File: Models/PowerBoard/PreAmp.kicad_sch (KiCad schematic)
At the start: 14 parts, among them U5 LM7805, 5V, 5%, U6 LM7905, -5V, 5%

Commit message: Should be finished with components BOM
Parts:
- C10, C11: Cost (none) -> $0.078; Purchase Link (none) -> https://www.digikey.com/en/products/detail/murata-electroni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
- C12: Cost (none) -> $0.079; Purchase Link (none) -> https://www.digikey.com/en/products/detail/murata-electroni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
- C13, C14: Cost (none) -> $0.087; Purchase Link (none) -> https://www.digikey.com/en/products/detail/murata-electroni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
- C9: Cost (none) -> $0.074; Purchase Link (none) -> https://www.digikey.com/en/products/detail/murata-electroni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
- D11, D12: Cost (none) -> $0.166; Purchase Link (none) -> https://www.digikey.com/en/products/detail/diodes-incorpora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
- RV1, RV2: Cost (none) -> $2.050; Purchase Link (none) -> https://www.digikey.com/en/products/detail/bourns-inc/3296Y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
- U5: Cost (none) -> $1.800; Purchase Link (none) -> https://www.digikey.com/en/products/detail/texas-instrument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
- U6: Cost (none) -> $1.530; Purchase Link (none) -> https://www.digikey.com/en/products/detail/texas-instrument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
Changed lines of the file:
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@@
+			)
+		)
+		(property "Cost" "$0.078"
+			(at 106.68 118.11 0)
+			(effects
+				(font
+					(size 1.27 1.27)
+				)
+				(hide yes)
+			)
+		)
+		(property "Purchase Link" "https://www.digikey.com/en/products/detail/murata-electronics/GRT188R61H105KE13D/5416752"
+			(at 106.68 118.11 0)
+			(effects
+				(font
+					(size 1.27 1.27)
+				)
+				(hide yes)
 			)
 		)
@@
 			)
 		)
-		(property "Purchase Link" ""
+		(property "Purchase Link" "https://www.digikey.com/en/products/detail/texas-instruments/LM7805CT-NOPB/3901929"
+			(at 68.58 55.88 0)
+			(effects
+				(font
+					(size 1.27 1.27)
+				)
+				(hide yes)
+			)
+		)
+		(property "Cost" "$1.800"
 			(at 68.58 55.88 0)
 			(effects
@@
 			)
 		)
-		(property "Purchase Link" ""
+		(property "Purchase Link" "https://www.digikey.com/en/products/detail/diodes-incorporated/1N5819HW-7-F/814970"
 			(at 129.54 118.11 0)
+			(effects
+				(font
+					(size 1.27 1.27)
+				)
+				(hide yes)
+			)
+		)
+		(property "Cost" "$0.166"
+			(at 129.54 118.11 90)
 			(effects
 				(font
@@
 			)
 		)
-		(property "Purchase Link" ""
+		(property "Purchase Link" "https://www.digikey.com/en/products/detail/murata-electronics/GRT188R61H105KE13D/5416752"
+			(at 106.68 148.59 0)
+			(effects
+				(font
+					(size 1.27 1.27)
+				)
+				(hide yes)
+			)
+		)
+		(property "Cost" "$0.078"
 			(at 106.68 148.59 0)
 			(effects
@@
 			)
 		)
+		(property "Cost" "$0.087"
+			(at 210.82 57.15 0)
+			(effects
+				(font
+					(size 1.27 1.27)
+				)
+				(hide yes)
+			)
+		)
+		(property "Purchase Link" "https://www.digikey.com/en/products/detail/murata-electronics/GRM21BR61E106KA73K/4905532"
+			(at 210.82 57.15 0)
+			(effects
+				(font
+					(size 1.27 1.27)
+				)
+				(hide yes)
+			)
+		)
 		(pin "1"
 		)
@@
 			)
 		)
+		(property "Cost" "$0.079"
+			(at 114.3 67.31 0)
+			(effects
+				(font
+					(size 1.27 1.27)
+				)
+				(hide yes)
+			)
+		)
+		(property "Purchase Link" "https://www.digikey.com/en/products/detail/murata-electronics/GRM188R72A104KA35D/702549"
+			(at 114.3 67.31 0)
+			(effects
+				(font
+					(size 1.27 1.27)
+				)
+				(hide yes)
+			)
+		)
 		(pin "1"
 		)
@@
 			)
 		)
-		(property "Purchase Link" ""
+		(property "Purchase Link" "https://www.digikey.com/en/products/detail/texas-instruments/LM7905CT-NOPB/6349"
+			(at 68.58 132.08 0)
+			(effects
+				(font
+					(size 1.27 1.27)
+				)
+				(hide yes)
+			)
+		)
+		(property "Cost" "$1.530"
 			(at 68.58 132.08 0)
 			(effects
@@
 			)
 		)
+		(property "Cost" "$0.074"
+			(at 66.04 67.31 0)
+			(effects
+				(font
+					(size 1.27 1.27)
+				)
+				(hide yes)
+			)
+		)
+		(property "Purchase Link" "https://www.digikey.com/en/products/detail/murata-electronics/GRM188R71H224KAC4D/5797498"
+			(at 66.04 67.31 0)
+			(effects
+				(font
+					(size 1.27 1.27)
+				)
+				(hide yes)
+			)
+		)
 		(pin "1"
 		)
@@
 		)
 		(property "Description" "Unpolarized capacitor"
+			(at 210.82 110.49 0)
+			(effects
+				(font
+					(size 1.27 1.27)
+				)
+				(hide yes)
+			)
+		)
+		(property "Cost" "$0.087"
+			(at 210.82 110.49 0)
+			(effects
+				(font
+					(size 1.27 1.27)
+				)
+				(hide yes)
+			)
+		)
+		(property "Purchase Link" "https://www.digikey.com/en/products/detail/murata-electronics/GRM21BR61E106KA73K/4905532"
 			(at 210.82 110.49 0)
 			(effects
@@
 			)
 		)
-		(property "Purchase Link" ""
+		(property "Purchase Link" "https://www.digikey.com/en/products/detail/diodes-incorporated/1N5819HW-7-F/814970"
 			(at 137.16 67.31 0)
+			(effects
+				(font
+					(size 1.27 1.27)
+				)
+				(hide yes)
+			)
+		)
+		(property "Cost" "$0.166"
+			(at 137.16 67.31 90)
 			(effects
 				(font
@@
 			)
 		)
+		(property "Cost" "$2.050"
+			(at 203.2 50.8 0)
+			(effects
+				(font
+					(size 1.27 1.27)
+				)
+				(hide yes)
+			)
+		)
+		(property "Purchase Link" "https://www.digikey.com/en/products/detail/bourns-inc/3296Y-1-102LF/1088084"
+			(at 203.2 50.8 0)
+			(effects
+				(font
+					(size 1.27 1.27)
+				)
+				(hide yes)
+			)
+		)
 		(pin "2"
 		)
@@
 			(at 203.2 116.84 0)
 			(effects
+				(font
+					(size 1.27 1.27)
+				)
+				(hide yes)
+			)
+		)
+		(property "Cost" "$2.050"
+			(at 203.2 116.84 0)
+			(effects
+				(font
+					(size 1.27 1.27)
+				)
+				(hide yes)
+			)
+		)
+		(property "Purchase Link" "https://www.digikey.com/en/products/detail/bourns-inc/3296Y-1-102LF/1088084"
+			(at 203.2 116.84 0)
+			(effects

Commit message: Assigned footprints
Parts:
- C10, C11, C12, C9: footprint (none) -> TwoTerminal:CAPC0603
- C13, C14: footprint (none) -> TwoTerminal:CAPC0805
- D10, D9: footprint (none) -> TwoTerminal:SOD-123FL
- D11, D12: footprint (none) -> TwoTerminal:SOD-123
- RV1, RV2: footprint (none) -> ThreeTerminal:Bourns_3296Y
- U5, U6: footprint (none) -> ThreeTerminal:TO-220
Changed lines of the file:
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@@
 			)
 		)
-		(property "Footprint" ""
+		(property "Footprint" "TwoTerminal:CAPC0603"
 			(at 107.6452 121.92 0)
 			(effects
@@
 			)
 		)
-		(property "Footprint" ""
+		(property "Footprint" "ThreeTerminal:TO-220"
 			(at 68.58 55.88 0)
 			(effects
@@
 			)
 		)
-		(property "Footprint" ""
+		(property "Footprint" "TwoTerminal:SOD-123"
 			(at 129.54 118.11 0)
 			(effects
@@
 			)
 		)
-		(property "Footprint" ""
+		(property "Footprint" "TwoTerminal:CAPC0603"
 			(at 107.6452 152.4 0)
 			(effects
@@
 			)
 		)
-		(property "Footprint" ""
+		(property "Footprint" "TwoTerminal:CAPC0805"
 			(at 211.7852 60.96 0)
 			(effects
@@
 			)
 		)
-		(property "Footprint" ""
+		(property "Footprint" "TwoTerminal:SOD-123FL"
 			(at 86.36 38.1 0)
 			(effects
@@
 			)
 		)
-		(property "Footprint" ""
+		(property "Footprint" "TwoTerminal:SOD-123FL"
 			(at 111.76 135.89 0)
 			(effects
@@
 			)
 		)
-		(property "Footprint" ""
+		(property "Footprint" "TwoTerminal:CAPC0603"
 			(at 115.2652 71.12 0)
 			(effects
@@
 			)
 		)
-		(property "Footprint" ""
+		(property "Footprint" "ThreeTerminal:TO-220"
 			(at 68.58 132.08 0)
 			(effects
@@
 			)
 		)
-		(property "Footprint" ""
+		(property "Footprint" "TwoTerminal:CAPC0603"
 			(at 67.0052 71.12 0)
 			(effects
@@
 			)
 		)
-		(property "Footprint" ""
+		(property "Footprint" "TwoTerminal:CAPC0805"
 			(at 211.7852 114.3 0)
 			(effects
@@
 			)
 		)
-		(property "Footprint" ""
+		(property "Footprint" "TwoTerminal:SOD-123"
 			(at 137.16 67.31 0)
 			(effects
@@
 			)
 		)
-		(property "Footprint" ""
+		(property "Footprint" "ThreeTerminal:Bourns_3296Y"
 			(at 203.2 50.8 0)
 			(effects
@@
 			)
 		)
-		(property "Footprint" ""
+		(property "Footprint" "ThreeTerminal:Bourns_3296Y"
 			(at 203.2 116.84 0)
 			(effects

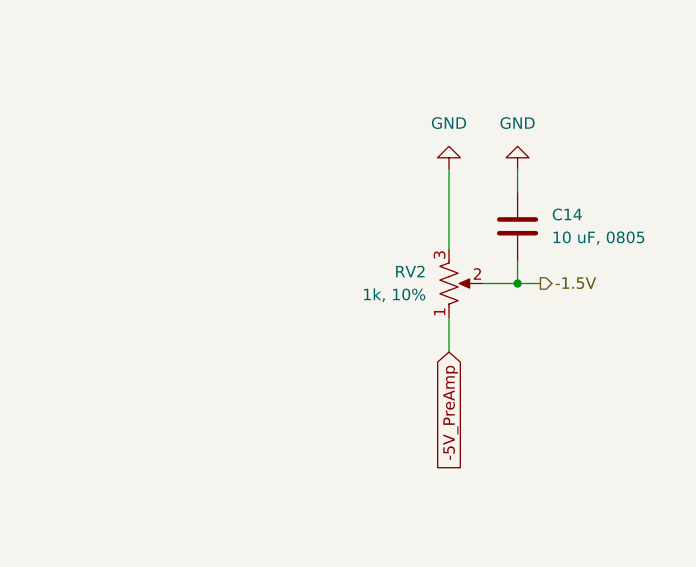
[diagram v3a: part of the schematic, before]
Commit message: Everything is now aligned very well on the power board
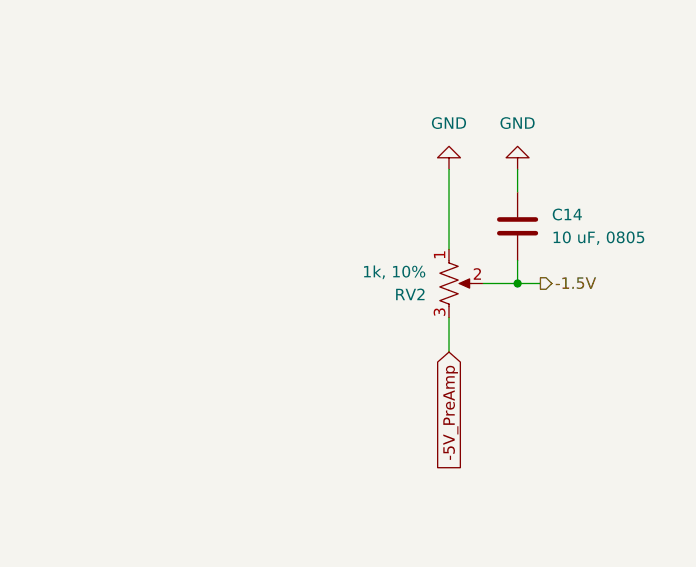
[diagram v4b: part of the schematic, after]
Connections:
- net -5V_PreAmp: now also RV2.3; no longer RV2.1
- net GND: now also RV2.1; no longer RV2.3
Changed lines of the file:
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@@
 		(on_board yes)
 		(dnp no)
-		(property "Reference" "#PWR045"
+		(property "Reference" "#PWR044"
 			(at 203.2 69.85 0)
 			(effects
@@
 			(project "PowerBoard"
 				(path "/c19e9b7b-7f36-470c-862a-1a648d3f14f6/55f1d4dd-dd9a-4f22-90c5-bff482123087"
-					(reference "#PWR045")
+					(reference "#PWR044")
 					(unit 1)
 				)
@@
 		(dnp no)
 		(fields_autoplaced yes)
-		(property "Reference" "#PWR037"
+		(property "Reference" "#PWR036"
 			(at 66.04 80.01 0)
 			(effects
@@
 			(project ""
 				(path "/c19e9b7b-7f36-470c-862a-1a648d3f14f6/55f1d4dd-dd9a-4f22-90c5-bff482123087"
-					(reference "#PWR037")
+					(reference "#PWR036")
 					(unit 1)
 				)
@@
 		(dnp no)
 		(fields_autoplaced yes)
-		(property "Reference" "#PWR043"
+		(property "Reference" "#PWR042"
 			(at 129.54 105.41 0)
 			(effects
@@
 			(project "PowerBoard"
 				(path "/c19e9b7b-7f36-470c-862a-1a648d3f14f6/55f1d4dd-dd9a-4f22-90c5-bff482123087"
-					(reference "#PWR043")
+					(reference "#PWR042")
 					(unit 1)
 				)
@@
 		(dnp no)
 		(fields_autoplaced yes)
-		(property "Reference" "#PWR048"
+		(property "Reference" "#PWR047"
 			(at 210.82 97.79 0)
 			(effects
@@
 			(project "PowerBoard"
 				(path "/c19e9b7b-7f36-470c-862a-1a648d3f14f6/55f1d4dd-dd9a-4f22-90c5-bff482123087"
-					(reference "#PWR048")
+					(reference "#PWR047")
 					(unit 1)
 				)
@@
 		(dnp no)
 		(fields_autoplaced yes)
-		(property "Reference" "#PWR041"
+		(property "Reference" "#PWR040"
 			(at 106.68 161.29 0)
 			(effects
@@
 			(project "PowerBoard"
 				(path "/c19e9b7b-7f36-470c-862a-1a648d3f14f6/55f1d4dd-dd9a-4f22-90c5-bff482123087"
-					(reference "#PWR041")
+					(reference "#PWR040")
 					(unit 1)
 				)
@@
 		(dnp no)
 		(fields_autoplaced yes)
-		(property "Reference" "#PWR042"
+		(property "Reference" "#PWR041"
 			(at 114.3 80.01 0)
 			(effects
@@
 			(project "PowerBoard"
 				(path "/c19e9b7b-7f36-470c-862a-1a648d3f14f6/55f1d4dd-dd9a-4f22-90c5-bff482123087"
-					(reference "#PWR042")
+					(reference "#PWR041")
 					(unit 1)
 				)
@@
 		(dnp no)
 		(fields_autoplaced yes)
-		(property "Reference" "#PWR038"
+		(property "Reference" "#PWR037"
 			(at 62.23 132.08 0)
 			(effects
@@
 			(project "PowerBoard"
 				(path "/c19e9b7b-7f36-470c-862a-1a648d3f14f6/55f1d4dd-dd9a-4f22-90c5-bff482123087"
-					(reference "#PWR038")
+					(reference "#PWR037")
 					(unit 1)
 				)
@@
 		(dnp no)
 		(fields_autoplaced yes)
-		(property "Reference" "#PWR046"
+		(property "Reference" "#PWR045"
 			(at 203.2 97.79 0)
 			(effects
@@
 			(project "PowerBoard"
 				(path "/c19e9b7b-7f36-470c-862a-1a648d3f14f6/55f1d4dd-dd9a-4f22-90c5-bff482123087"
-					(reference "#PWR046")
+					(reference "#PWR045")
 					(unit 1)
 				)
@@
 		(dnp no)
 		(fields_autoplaced yes)
-		(property "Reference" "#PWR040"
+		(property "Reference" "#PWR039"
 			(at 106.68 105.41 0)
 			(effects
@@
 			(project "PowerBoard"
 				(path "/c19e9b7b-7f36-470c-862a-1a648d3f14f6/55f1d4dd-dd9a-4f22-90c5-bff482123087"
-					(reference "#PWR040")
+					(reference "#PWR039")
 					(unit 1)
 				)
@@
 		(dnp no)
 		(fields_autoplaced yes)
-		(property "Reference" "#PWR039"
+		(property "Reference" "#PWR038"
 			(at 110.49 58.42 0)
 			(effects
@@
 			(project "PowerBoard"
 				(path "/c19e9b7b-7f36-470c-862a-1a648d3f14f6/55f1d4dd-dd9a-4f22-90c5-bff482123087"
-					(reference "#PWR039")
+					(reference "#PWR038")
 					(unit 1)
 				)
@@
 		(dnp no)
 		(fields_autoplaced yes)
-		(property "Reference" "#PWR047"
+		(property "Reference" "#PWR046"
 			(at 210.82 69.85 0)
 			(effects
@@
 			(project "PowerBoard"
 				(path "/c19e9b7b-7f36-470c-862a-1a648d3f14f6/55f1d4dd-dd9a-4f22-90c5-bff482123087"
-					(reference "#PWR047")
+					(reference "#PWR046")
 					(unit 1)
 				)
@@
 		(lib_id "Device:R_Potentiometer_US")
 		(at 203.2 116.84 0)
-		(mirror x)
 		(unit 1)
 		(exclude_from_sim no)
@@
 		(dnp no)
 		(property "Reference" "RV2"
-			(at 200.66 115.5699 0)
+			(at 200.66 118.1101 0)
 			(effects
 				(font
@@
 		)
 		(property "Value" "1k, 10%"
-			(at 200.66 118.1099 0)
+			(at 200.66 115.5701 0)
 			(effects
 				(font
@@
 		(dnp no)
 		(fields_autoplaced yes)
-		(property "Reference" "#PWR044"
+		(property "Reference" "#PWR043"
 			(at 137.16 80.01 0)
 			(effects
@@
 			(project "PowerBoard"
 				(path "/c19e9b7b-7f36-470c-862a-1a648d3f14f6/55f1d4dd-dd9a-4f22-90c5-bff482123087"
-					(reference "#PWR044")
-					(unit 1)
-				)
+					(reference "#PWR043")
+					(unit 1)
+				)

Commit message: Save progress
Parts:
- C10, C11, C12, C13, C14, C9, D11, D12, U5, U6: now left out of the parts list
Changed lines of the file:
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@@
 		(unit 1)
 		(exclude_from_sim no)
-		(in_bom yes)
+		(in_bom no)
 		(on_board yes)
 		(dnp no)
@@
 		(unit 1)
 		(exclude_from_sim no)
-		(in_bom yes)
+		(in_bom no)
 		(on_board yes)
 		(dnp no)
@@
 		(unit 1)
 		(exclude_from_sim no)
-		(in_bom yes)
+		(in_bom no)
 		(on_board yes)
 		(dnp no)
@@
 		(unit 1)
 		(exclude_from_sim no)
-		(in_bom yes)
+		(in_bom no)
 		(on_board yes)
 		(dnp no)
@@
 		(unit 1)
 		(exclude_from_sim no)
-		(in_bom yes)
+		(in_bom no)
 		(on_board yes)
 		(dnp no)
@@
 		(unit 1)
 		(exclude_from_sim no)
-		(in_bom yes)
+		(in_bom no)
 		(on_board yes)
 		(dnp no)
@@
 		(unit 1)
 		(exclude_from_sim no)
-		(in_bom yes)
+		(in_bom no)
 		(on_board yes)
 		(dnp no)
@@
 		(unit 1)
 		(exclude_from_sim no)
-		(in_bom yes)
+		(in_bom no)
 		(on_board yes)
 		(dnp no)
@@
 		(unit 1)
 		(exclude_from_sim no)
-		(in_bom yes)
+		(in_bom no)
 		(on_board yes)
 		(dnp no)
@@
 		(unit 1)
 		(exclude_from_sim no)
-		(in_bom yes)
-		(on_board yes)
-		(dnp no)
+		(in_bom no)
+		(on_board yes)
+		(dnp no)
